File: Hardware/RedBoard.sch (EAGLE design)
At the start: 65 parts, among them IC3 LM1117, J1 POWER_JACKOVERPASTE_REDBOARD_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, J2 ICSP, Q1 ZXMP6A13FTA, Q2 2N7002PW, U1 FT231XS, U2 MIC5205, U3 ATMEGA328, Y1 16MHz

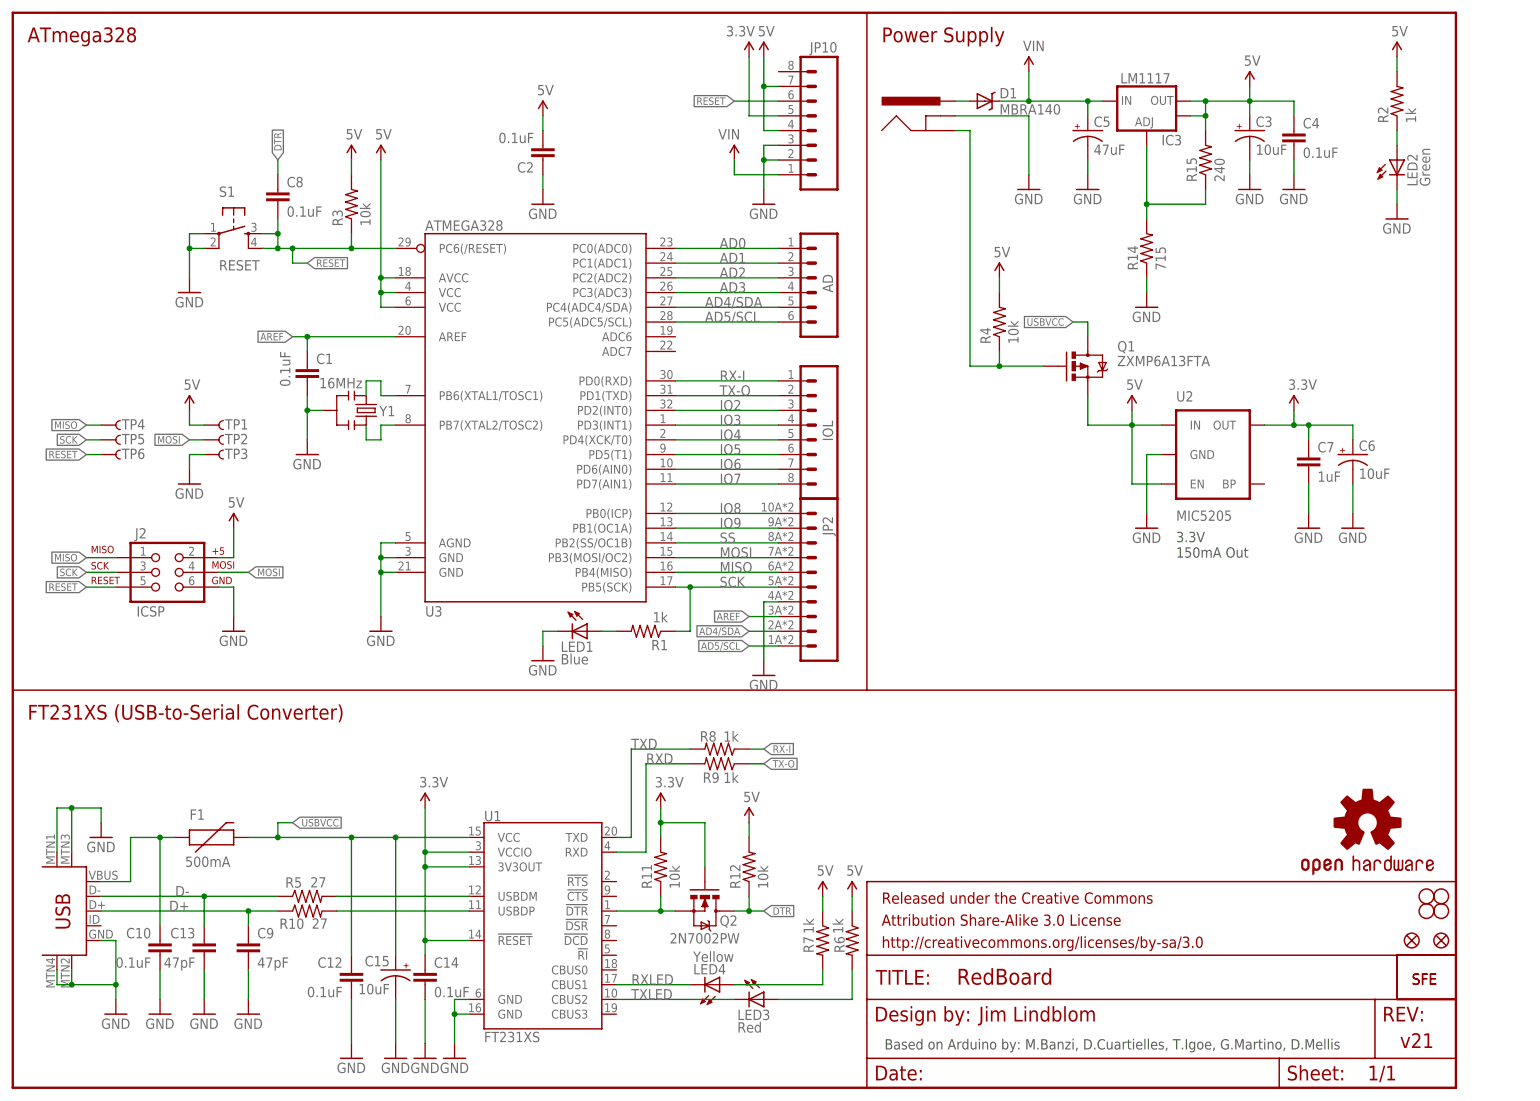
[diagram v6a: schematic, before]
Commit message: Adjustments to FT231X circuit. Package updates.
- Disconnecting FTDI 3.3V (VCCIO) from ATmega328's 3.3V bus
- Getting rid of MOSFET on DTR line. 5V, 10k pull-up does the job just
fine.
- Adding vias to ISP test points.
- Tailing the dimensions of the board in a bit. Board is now
Arduino-standard 2.1" tall (was 2.14")
- Updating 1x10, 1x08, and 1x06 packages to minimize false DRC errors.
- Updating these packages for QC: resonator, MBRA140 diode, PTC, barrel
jack, reset button.
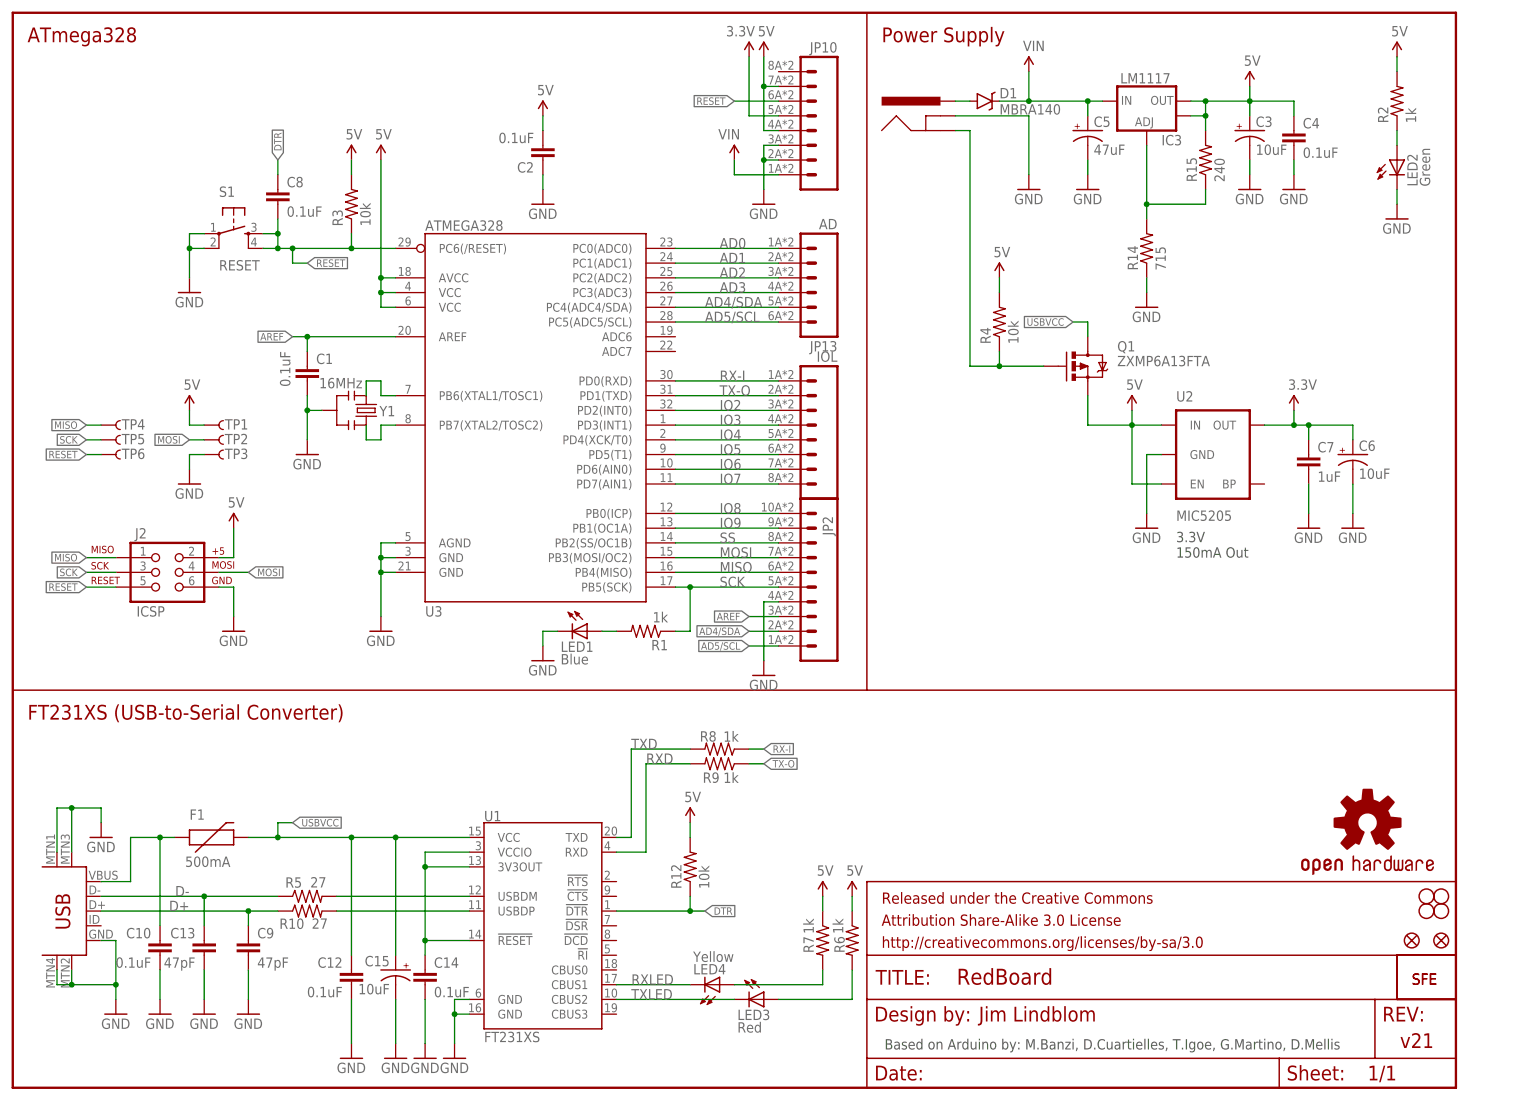
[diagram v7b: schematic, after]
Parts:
- removed AD: (no value), SparkFun:M06SMD-STRAIGHT-COMBO
- removed IOL: (no value), SparkFun:M08SMD-COMBO
- removed J1: POWER_JACKOVERPASTE_REDBOARD_0603, Testing:POWER_JACKOVERPASTE_REDBOARD_0603
- removed Q2: 2N7002PW, SparkFun-DiscreteSemi:MOSFET-NCHANNEL2N7002PW
- removed R11: 10k, SparkFun:RESISTOR0603-RES
- added J3: POWER_JACKSUPER_BOMB_DIGITY, Testing:POWER_JACKSUPER_BOMB_DIGITY
- added JP11: IOL, SparkFun-Connectors:M08SMD-COMBO
- added JP13: AD, SparkFun-Connectors:M06SMD-STRAIGHT-COMBO
- D1: device SparkFun:DIODE-SCHOTTKY_ -> SparkFun-DiscreteSemi:MBRA140
- F1: device SparkFun:PTCSMD -> SparkFun-PowerIC:PTCSMD
- S1: device SparkFun:TAC_SWITCHSMD -> SparkFun-Electromechanical:TAC_SWITCHSMD
- Y1: device SparkFun-FreqCtrl:RESONATORSMD -> SparkFun-FreqCtrl:RESONATOR16MHZ
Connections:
- removed net N$12: Q2.S, R11.1, U1.!DTR
- new net 3V3_FTDI: C14.1, U1.!RESET, U1.3V3OUT, U1.VCCIO
- net 3.3V: no longer C14.1, Q2.G, R11.2, U1.!RESET, U1.3V3OUT, U1.VCCIO
- net AD0: now also JP13.1; no longer AD.1
- net AD1: now also JP13.2; no longer AD.2
- net AD2: now also JP13.3; no longer AD.3
- net AD3: now also JP13.4; no longer AD.4
- net AD4/SDA: now also JP13.5; no longer AD.5
- net AD5/SCL: now also JP13.6; no longer AD.6
- net DTR: now also U1.!DTR; no longer Q2.D
- net GND: now also J3.GNDBREAK; no longer J1.GNDBREAK
- net INSERT: now also J3.GND; no longer J1.GND
- net IO2: now also JP11.3; no longer IOL.3
- net IO3: now also JP11.4; no longer IOL.4
- net IO4: now also JP11.5; no longer IOL.5
- net IO5: now also JP11.6; no longer IOL.6
- net IO6: now also JP11.7; no longer IOL.7
- net IO7: now also JP11.8; no longer IOL.8
- net PWRIN: now also J3.PWR; no longer J1.PWR
- net RX-I: now also JP11.1; no longer IOL.1
- net TX-O: now also JP11.2; no longer IOL.2
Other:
- moved on the sheet: JP10, R12

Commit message: upping version number to v22`
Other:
- note added: "v22"
- note removed: "v21"
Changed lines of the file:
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@@
 <?xml version="1.0" encoding="utf-8"?>
 <!DOCTYPE eagle SYSTEM "eagle.dtd">
-<eagle version="6.5.0">
+<eagle version="6.6.0">
 <drawing>
 <settings>
@@
 <grid distance="0.1" unitdist="inch" unit="inch" style="lines" multiple="1" display="no" altdistance="0.01" altunitdist="inch" altunit="inch"/>
 <layers>
-<layer number="1" name="Top" color="4" fill="1" visible="yes" active="no"/>
-<layer number="2" name="Route2" color="1" fill="3" visible="yes" active="no"/>
-<layer number="3" name="Route3" color="4" fill="3" visible="yes" active="no"/>
-<layer number="4" name="Route4" color="1" fill="4" visible="yes" active="no"/>
-<layer number="5" name="Route5" color="4" fill="4" visible="yes" active="no"/>
-<layer number="6" name="Route6" color="1" fill="8" visible="yes" active="no"/>
-<layer number="7" name="Route7" color="4" fill="8" visible="yes" active="no"/>
-<layer number="8" name="Route8" color="1" fill="2" visible="yes" active="no"/>
-<layer number="9" name="Route9" color="4" fill="2" visible="yes" active="no"/>
-<layer number="10" name="Route10" color="1" fill="7" visible="yes" active="no"/>
-<layer number="11" name="Route11" color="4" fill="7" visible="yes" active="no"/>
-<layer number="12" name="Route12" color="1" fill="5" visible="yes" active="no"/>
-<layer number="13" name="Route13" color="4" fill="5" visible="yes" active="no"/>
-<layer number="14" name="Route14" color="1" fill="6" visible="yes" active="no"/>
-<layer number="15" name="Route15" color="4" fill="6" visible="yes" active="no"/>
-<layer number="16" name="Bottom" color="1" fill="1" visible="yes" active="no"/>
-<layer number="17" name="Pads" color="2" fill="1" visible="yes" active="no"/>
-<layer number="18" name="Vias" color="2" fill="1" visible="yes" active="no"/>
-<layer number="19" name="Unrouted" color="6" fill="1" visible="yes" active="no"/>
-<layer number="20" name="Dimension" color="15" fill="1" visible="yes" active="no"/>
-<layer number="21" name="tPlace" color="16" fill="1" visible="yes" active="no"/>
-<layer number="22" name="bPlace" color="14" fill="1" visible="yes" active="no"/>
-<layer number="23" name="tOrigins" color="15" fill="1" visible="yes" active="no"/>
-<layer number="24" name="bOrigins" color="15" fill="1" visible="yes" active="no"/>
-<layer number="25" name="tNames" color="7" fill="1" visible="yes" active="no"/>
-<layer number="26" name="bNames" color="7" fill="1" visible="yes" active="no"/>
-<layer number="27" name="tValues" color="7" fill="1" visible="yes" active="no"/>
-<layer number="28" name="bValues" color="7" fill="1" visible="yes" active="no"/>
+<layer number="1" name="Top" color="4" fill="1" visible="no" active="no"/>
+<layer number="2" name="Route2" color="1" fill="3" visible="no" active="no"/>
+<layer number="3" name="Route3" color="4" fill="3" visible="no" active="no"/>
+<layer number="4" name="Route4" color="1" fill="4" visible="no" active="no"/>
+<layer number="5" name="Route5" color="4" fill="4" visible="no" active="no"/>
+<layer number="6" name="Route6" color="1" fill="8" visible="no" active="no"/>
+<layer number="7" name="Route7" color="4" fill="8" visible="no" active="no"/>
+<layer number="8" name="Route8" color="1" fill="2" visible="no" active="no"/>
+<layer number="9" name="Route9" color="4" fill="2" visible="no" active="no"/>
+<layer number="10" name="Route10" color="1" fill="7" visible="no" active="no"/>
+<layer number="11" name="Route11" color="4" fill="7" visible="no" active="no"/>
+<layer number="12" name="Route12" color="1" fill="5" visible="no" active="no"/>
+<layer number="13" name="Route13" color="4" fill="5" visible="no" active="no"/>
+<layer number="14" name="Route14" color="1" fill="6" visible="no" active="no"/>
+<layer number="15" name="Route15" color="4" fill="6" visible="no" active="no"/>
+<layer number="16" name="Bottom" color="1" fill="1" visible="no" active="no"/>
+<layer number="17" name="Pads" color="2" fill="1" visible="no" active="no"/>
+<layer number="18" name="Vias" color="2" fill="1" visible="no" active="no"/>
+<layer number="19" name="Unrouted" color="6" fill="1" visible="no" active="no"/>
+<layer number="20" name="Dimension" color="15" fill="1" visible="no" active="no"/>
+<layer number="21" name="tPlace" color="16" fill="1" visible="no" active="no"/>
+<layer number="22" name="bPlace" color="14" fill="1" visible="no" active="no"/>
+<layer number="23" name="tOrigins" color="15" fill="1" visible="no" active="no"/>
+<layer number="24" name="bOrigins" color="15" fill="1" visible="no" active="no"/>
+<layer number="25" name="tNames" color="7" fill="1" visible="no" active="no"/>
+<layer number="26" name="bNames" color="7" fill="1" visible="no" active="no"/>
+<layer number="27" name="tValues" color="7" fill="1" visible="no" active="no"/>
+<layer number="28" name="bValues" color="7" fill="1" visible="no" active="no"/>
 <layer number="29" name="tStop" color="2" fill="3" visible="no" active="no"/>
 <layer number="30" name="bStop" color="5" fill="6" visible="no" active="no"/>
@@
 <layer number="35" name="tGlue" color="7" fill="4" visible="no" active="no"/>
 <layer number="36" name="bGlue" color="7" fill="5" visible="no" active="no"/>
-<layer number="37" name="tTest" color="7" fill="1" visible="yes" active="no"/>
-<layer number="38" name="bTest" color="7" fill="1" visible="yes" active="no"/>
+<layer number="37" name="tTest" color="7" fill="1" visible="no" active="no"/>
+<layer number="38" name="bTest" color="7" fill="1" visible="no" active="no"/>
 <layer number="39" name="tKeepout" color="4" fill="11" visible="no" active="no"/>
 <layer number="40" name="bKeepout" color="1" fill="11" visible="no" active="no"/>
@@
 <layer number="44" name="Drills" color="7" fill="1" visible="no" active="no"/>
 <layer number="45" name="Holes" color="7" fill="1" visible="no" active="no"/>
-<layer number="46" name="Milling" color="3" fill="1" visible="yes" active="no"/>
-<layer number="47" name="Measures" color="7" fill="1" visible="yes" active="no"/>
-<layer number="48" name="Document" color="7" fill="1" visible="yes" active="no"/>
-<layer number="49" name="Reference" color="13" fill="1" visible="yes" active="no"/>
-<layer number="50" name="dxf" color="12" fill="1" visible="yes" active="no"/>
-<layer number="51" name="tDocu" color="6" fill="1" visible="yes" active="no"/>
-<layer number="52" name="bDocu" color="7" fill="1" visible="yes" active="no"/>
-<layer number="53" name="tGND_GNDA" color="7" fill="1" visible="yes" active="no"/>
-<layer number="54" name="bGND_GNDA" color="7" fill="1" visible="yes" active="no"/>
-<layer number="56" name="wert" color="7" fill="1" visible="yes" active="no"/>
-<layer number="57" name="tCAD" color="7" fill="1" visible="yes" active="no"/>
+<layer number="46" name="Milling" color="3" fill="1" visible="no" active="no"/>
+<layer number="47" name="Measures" color="7" fill="1" visible="no" active="no"/>
+<layer number="48" name="Document" color="7" fill="1" visible="no" active="no"/>
+<layer number="49" name="Reference" color="13" fill="1" visible="no" active="no"/>
+<layer number="50" name="dxf" color="12" fill="1" visible="no" active="no"/>
+<layer number="51" name="tDocu" color="6" fill="1" visible="no" active="no"/>
+<layer number="52" name="bDocu" color="7" fill="1" visible="no" active="no"/>
+<layer number="53" name="tGND_GNDA" color="7" fill="1" visible="no" active="no"/>
+<layer number="54" name="bGND_GNDA" color="7" fill="1" visible="no" active="no"/>
+<layer number="56" name="wert" color="7" fill="1" visible="no" active="no"/>
+<layer number="57" name="tCAD" color="7" fill="1" visible="no" active="no"/>
 <layer number="91" name="Nets" color="2" fill="1" visible="yes" active="yes"/>
 <layer number="92" name="Busses" color="1" fill="1" visible="yes" active="yes"/>
@@
 <wire x1="147.32" y1="68.58" x2="248.92" y2="68.58" width="0.254" layer="94"/>
 <text x="166.624" y="11.43" size="2.54" layer="94">Jim Lindblom</text>
-<text x="239.268" y="6.858" size="2.54" layer="94">v21</text>
+<text x="239.268" y="6.858" size="2.54" layer="94">v22</text>
 </plain>
 <instances>
